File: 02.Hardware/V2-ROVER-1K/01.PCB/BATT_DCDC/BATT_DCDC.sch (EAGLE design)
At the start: 61 parts, among them J1 DF40C-20DP-0.4V_51_, K1 FLEX11, Q1 NVTFS9D6P04M8LTAG, Q2 2N7002PW, Q5 2N7002PW, U1 MCP6071T-E/OT, U3 TPS55330RTET, U7 MCP6071T-E/OT

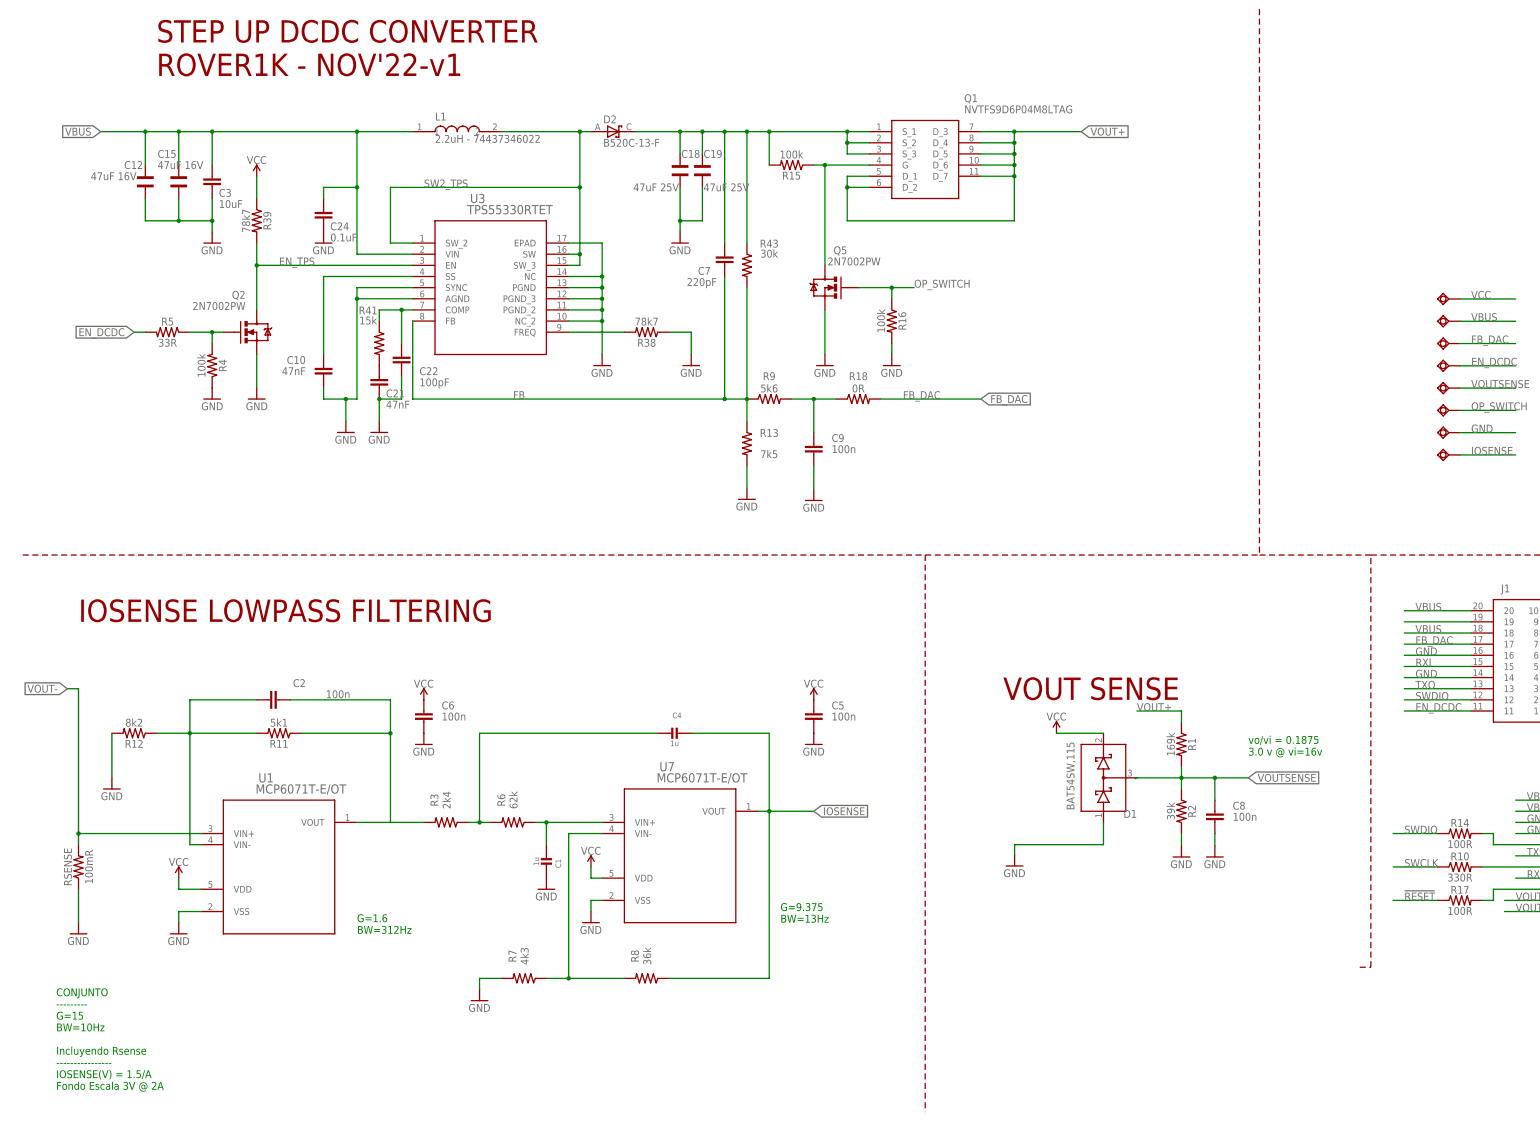
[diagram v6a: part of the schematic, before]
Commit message: Revision esquematico DCDC-release candidate para generar BOM 1ra produccion SETI
Pendiente de revisar serigrafias
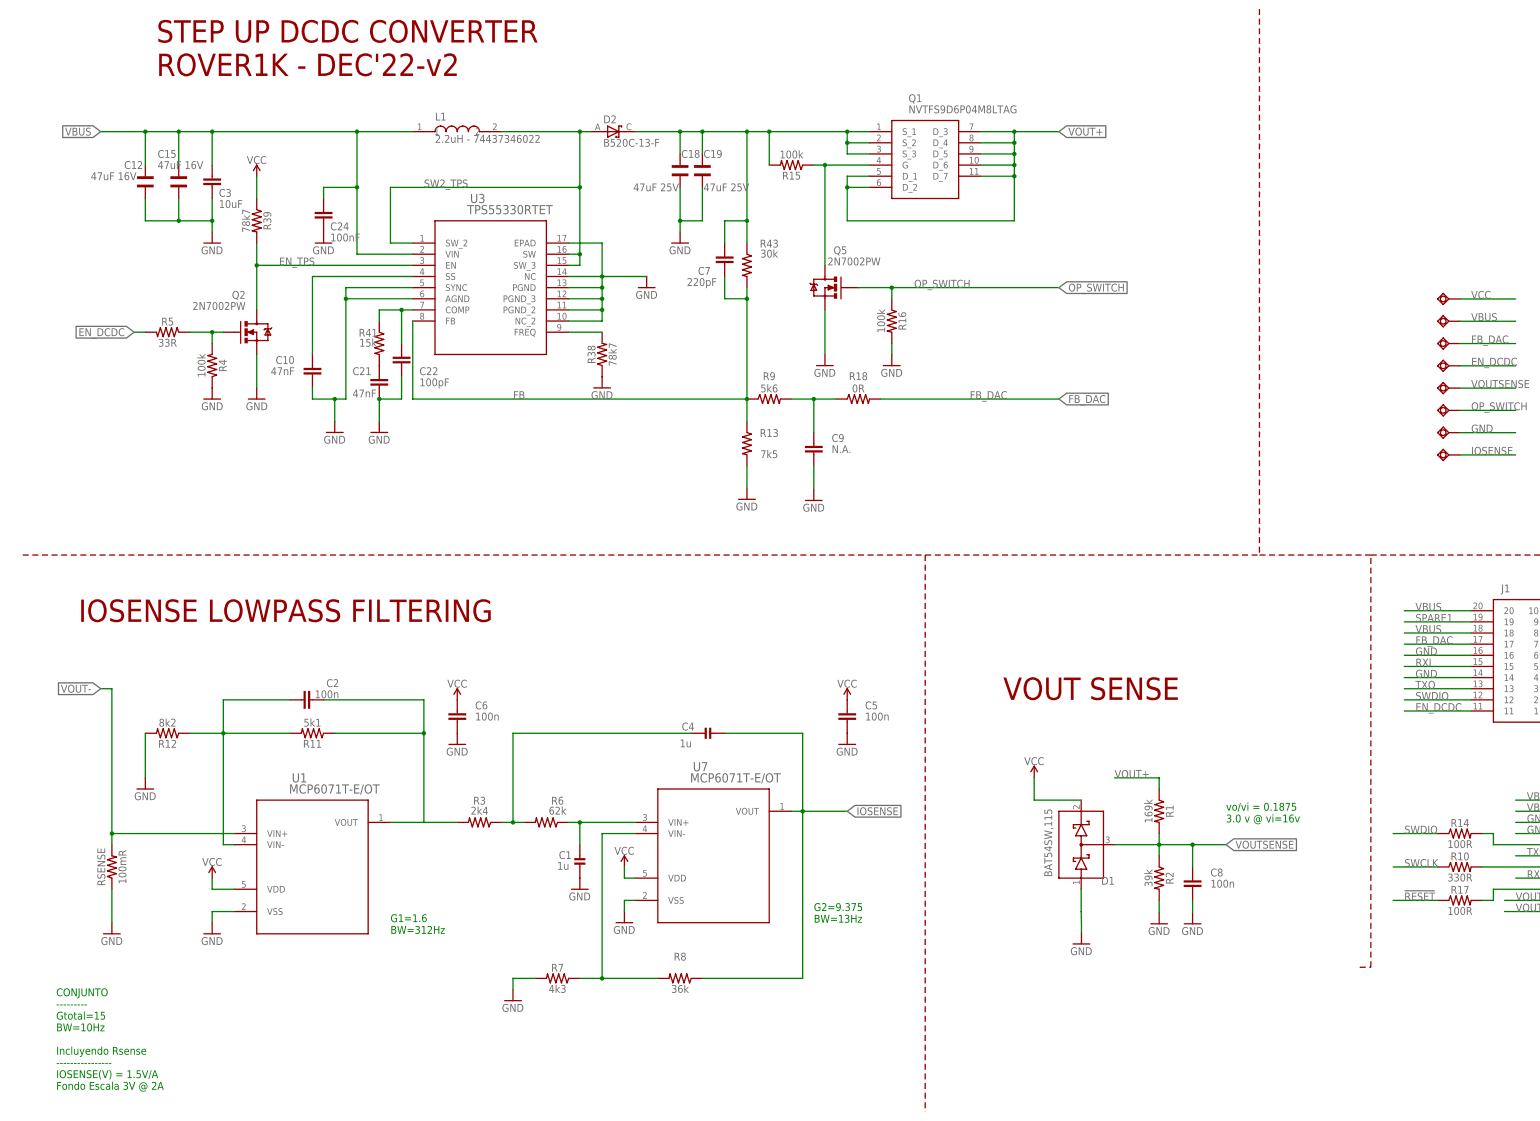
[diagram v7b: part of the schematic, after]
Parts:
- C24: value 0.1uF -> 100nF
- C9: value 100n -> N.A.
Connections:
- net N$9 renamed SPARE1
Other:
- note added: "CONJUNTO --------- Gtotal=15 BW=10Hz Incluyendo Rsense ---------------- IOSENSE(V) = 1.5V/A Fondo Escala 3V @ 2A"
- note added: "G1=1.6 BW=312Hz"
- note added: "G2=9.375 BW=13Hz"
- note added: "STEP UP DCDC CONVERTER ROVER1K - DEC'22-v2"
- note removed: "CONJUNTO --------- G=15 BW=10Hz Incluyendo Rsense ---------------- IOSENSE(V) = 1.5/A Fondo Escala 3V @ 2A"
- note removed: "G=1.6 BW=312Hz"
- note removed: "G=9.375 BW=13Hz"
- note removed: "STEP UP DCDC CONVERTER ROVER1K - NOV'22-v1"
- moved on the sheet: C1, C10, C2, C4, C5, C6, C8, D1, R1, R11, R12, R2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

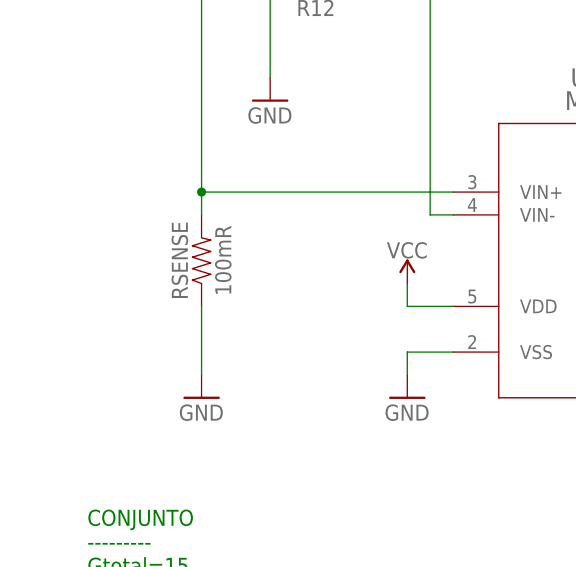
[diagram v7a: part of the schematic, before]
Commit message: Produccion 1 dic'22 - Se cambia RSENSE a 1206
Se cambia encapsulado 0603 por 1206
Se añaden más vias a la conexion de Rsense
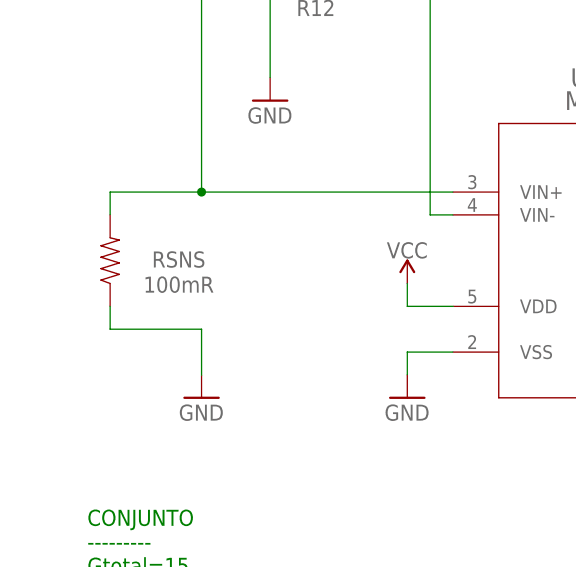
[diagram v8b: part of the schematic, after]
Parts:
- removed RSENSE: 100mR, SparkFun-Resistors:RESISTOR0603
- added RSNS: 100mR, SparkFun-Resistors:RESISTOR1206
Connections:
- net GND: now also RSNS.1; no longer RSENSE.1
- net VOUT-: now also RSNS.2; no longer RSENSE.2
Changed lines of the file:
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@@
 <part name="SUPPLY3" library="SparkFun-PowerSymbols" library_urn="urn:adsk.eagle:library:530" deviceset="VCC" device=""/>
 <part name="GND6" library="SparkFun" deviceset="GND" device=""/>
-<part name="RSENSE" library="SparkFun-Resistors" library_urn="urn:adsk.eagle:library:532" deviceset="RESISTOR" device="0603" package3d_urn="urn:adsk.eagle:package:39650/1" value="100mR"/>
 <part name="GND8" library="SparkFun" deviceset="GND" device=""/>
 <part name="C3" library="SparkFun-Capacitors" deviceset="10UF" device="-0805-10V-10%" value="10uF"/>
@@
 <part name="GND18" library="SparkFun" deviceset="GND" device=""/>
 <part name="C9" library="SparkFun-Capacitors" deviceset="0.1UF" device="-0603-25V-(+80/-20%)" value="N.A."/>
+<part name="RSNS" library="SparkFun-Resistors" library_urn="urn:adsk.eagle:library:532" deviceset="RESISTOR" device="1206" package3d_urn="urn:adsk.eagle:package:39654/1" value="100mR"/>
 </parts>
 <sheets>
@@
 <attribute name="VALUE" x="22.86" y="43.18" size="1.778" layer="96"/>
 </instance>
-<instance part="RSENSE" gate="G$1" x="25.4" y="60.96" smashed="yes" rot="R90">
-<attribute name="NAME" x="23.876" y="60.96" size="1.778" layer="95" font="vector" rot="R90" align="bottom-center"/>
-<attribute name="VALUE" x="26.924" y="60.96" size="1.778" layer="96" font="vector" rot="R90" align="top-center"/>
-</instance>
 <instance part="GND8" gate="1" x="33.02" y="78.74" smashed="yes">
 <attribute name="VALUE" x="30.48" y="76.2" size="1.778" layer="96"/>
@@
 <attribute name="NAME" x="189.484" y="159.639" size="1.778" layer="95" font="vector" rot="MR180"/>
 <attribute name="VALUE" x="189.484" y="157.099" size="1.778" layer="96" font="vector" rot="MR180"/>
+</instance>
+<instance part="RSNS" gate="G$1" x="15.24" y="60.96" smashed="yes" rot="R90">
+<attribute name="NAME" x="22.86" y="61.976" size="1.778" layer="95" font="vector" rot="R180" align="bottom-center"/>
+<attribute name="VALUE" x="22.86" y="57.404" size="1.778" layer="96" font="vector" rot="R180" align="top-center"/>
 </instance>
 </instances>
@@
 <segment>
 <pinref part="GND6" gate="1" pin="GND"/>
-<wire x1="25.4" y1="48.26" x2="25.4" y2="55.88" width="0.1524" layer="91"/>
-<pinref part="RSENSE" gate="G$1" pin="1"/>
+<wire x1="25.4" y1="48.26" x2="25.4" y2="53.34" width="0.1524" layer="91"/>
+<pinref part="RSNS" gate="G$1" pin="1"/>
+<wire x1="15.24" y1="55.88" x2="15.24" y2="53.34" width="0.1524" layer="91"/>
+<wire x1="15.24" y1="53.34" x2="25.4" y2="53.34" width="0.1524" layer="91"/>
 </segment>
 <segment>
@@
 <net name="VOUT-" class="0">
 <segment>
-<pinref part="RSENSE" gate="G$1" pin="2"/>
-<wire x1="25.4" y1="66.04" x2="25.4" y2="68.58" width="0.1524" layer="91"/>
 <wire x1="25.4" y1="68.58" x2="25.4" y2="101.6" width="0.1524" layer="91"/>
 <wire x1="25.4" y1="101.6" x2="22.86" y2="101.6" width="0.1524" layer="91"/>
@@
 <wire x1="53.34" y1="68.58" x2="25.4" y2="68.58" width="0.1524" layer="91"/>
 <junction x="25.4" y="68.58"/>
-</segment>
-<segment>
+<pinref part="RSNS" gate="G$1" pin="2"/>
+<wire x1="15.24" y1="66.04" x2="15.24" y2="68.58" width="0.1524" layer="91"/>
+<wire x1="15.24" y1="68.58" x2="25.4" y2="68.58" width="0.1524" layer="91"/>
+</segment>
+<segment>
